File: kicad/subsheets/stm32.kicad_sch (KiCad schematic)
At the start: 12 parts, among them U3 STM32U575RGT6

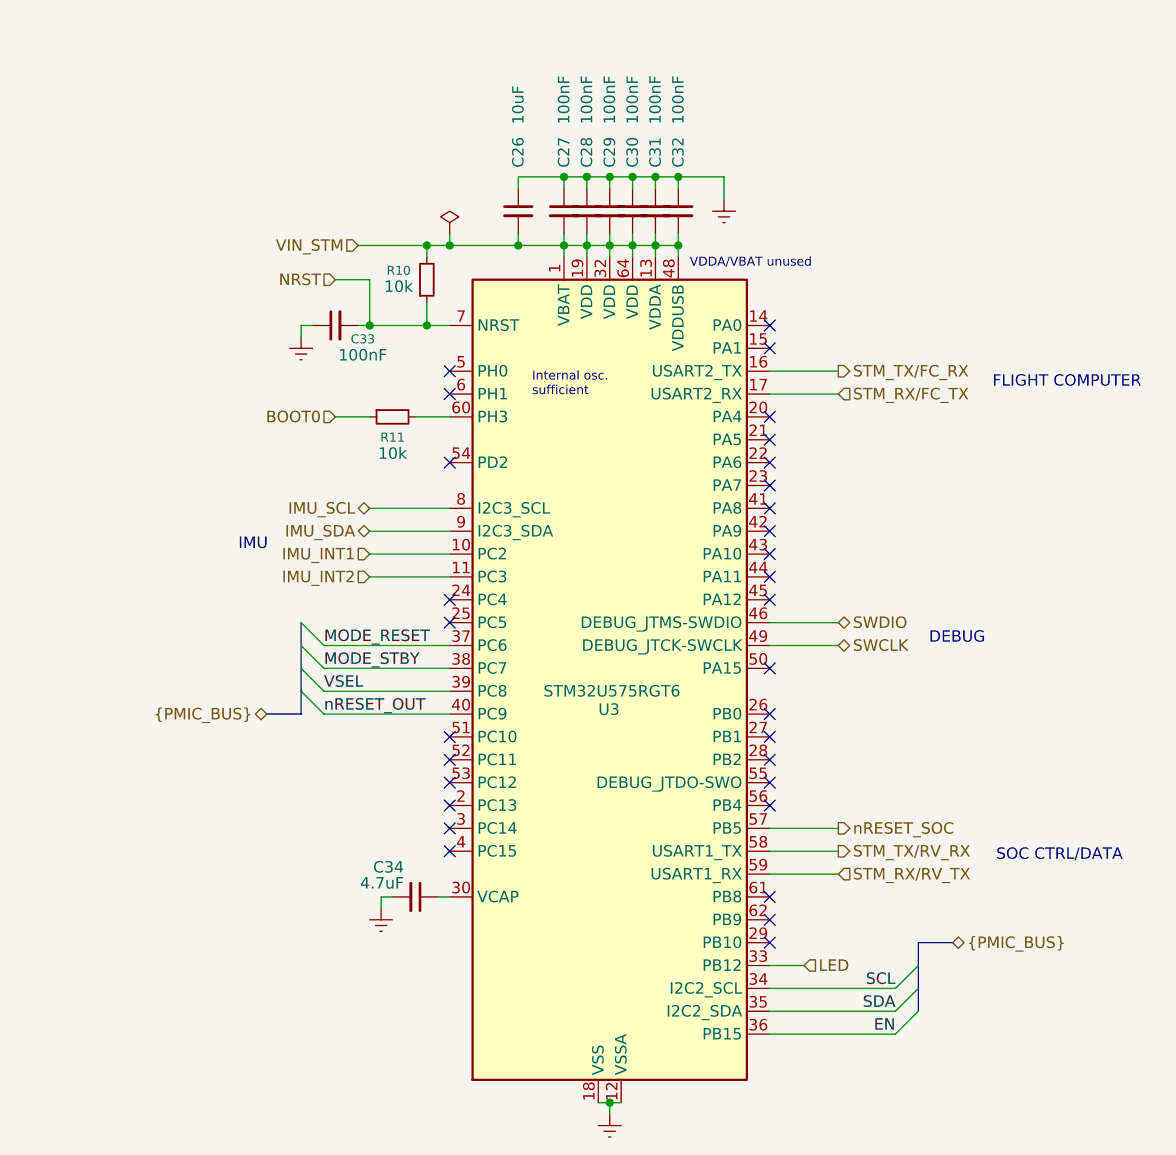
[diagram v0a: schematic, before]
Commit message: Switch to lower-cost STM32U0
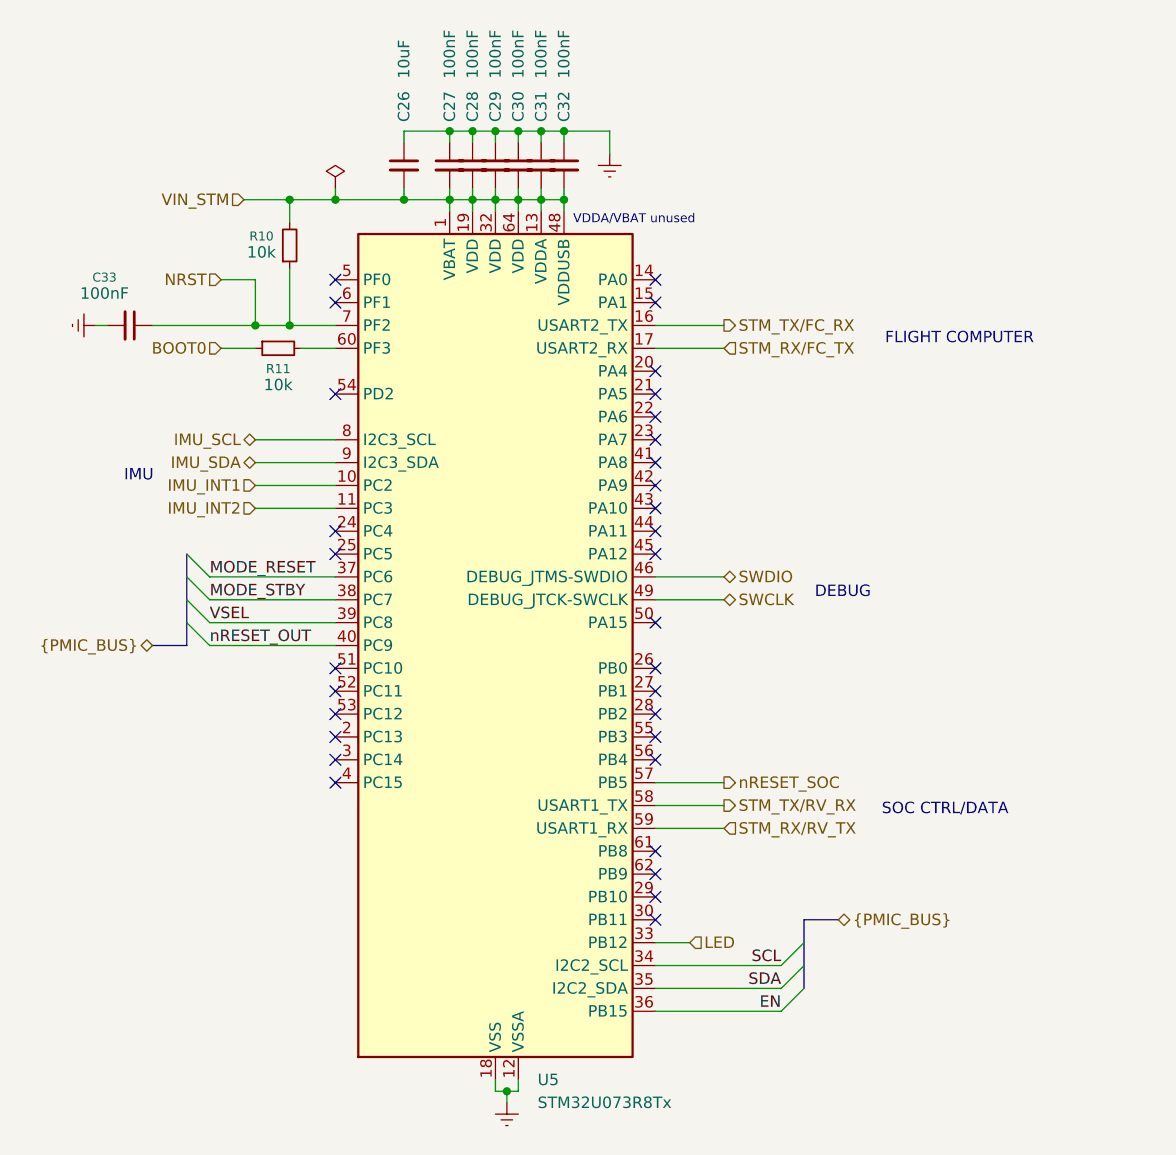
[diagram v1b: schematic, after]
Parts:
- removed C34: 4.7uF, Capacitor_SMD:C_0805_2012Metric, symbol Device:C_Small
- removed U3: STM32U575RGT6, Package_QFP:LQFP-64_10x10mm_P0.5mm, symbol MCU_ST_STM32U5:STM32U575RGTx
- added U5: STM32U073R8Tx, Package_QFP:LQFP-64_10x10mm_P0.5mm, symbol MCU_ST_STM32U0:STM32U073R8Tx
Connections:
- net EN: now also U5.36 (PB15)
- net GND: now also C33.2, U5.12 (VSSA), U5.18 (VSS), U5.31 (VSS), U5.47 (VSS), U5.63 (VSS); no longer C33.1
- net IMU_INT1: now also U5.10 (PC2)
- net IMU_INT2: now also U5.11 (PC3)
- net IMU_SCL: now also U5.8 (PC0)
- net IMU_SDA: now also U5.9 (PC1)
- net LED: now also U5.33 (PB12)
- net MODE_RESET: now also U5.37 (PC6)
- net MODE_STBY: now also U5.38 (PC7)
- net NRST: now also C33.1, U5.7 (PF2); no longer C33.2
- net SCL: now also U5.34 (PB13)
- net SDA: now also U5.35 (PB14)
- net STM_RX/FC_TX: now also U5.17 (PA3)
- net STM_RX/RV_TX: now also U5.59 (PB7)
- net STM_TX/FC_RX: now also U5.16 (PA2)
- net STM_TX/RV_RX: now also U5.58 (PB6)
- net SWCLK: now also U5.49 (PA14)
- net SWDIO: now also U5.46 (PA13)
- net VIN_STM: now also U5.1 (VBAT), U5.13 (VDDA), U5.19 (VDD), U5.32 (VDD), U5.48 (VDDUSB), U5.64 (VDD)
- net VSEL: now also U5.39 (PC8)
- net nRESET_OUT: now also U5.40 (PC9)
- net nRESET_SOC: now also U5.57 (PB5)
- net at R11.2: now also U5.60 (PF3)
- no-connect marks 31 -> 32
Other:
- note removed: "Internal osc. sufficient"
- moved on the sheet: C26, C27, C28, C29, C30, C31, C32, C33, R10, R11

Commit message: Add missing passives and microphone
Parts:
- renumbered U5 to U3
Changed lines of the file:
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@@
 	)
 	(junction
-		(at 127 49.53)
-		(diameter 0)
-		(color 0 0 0 0)
-	)
-	(junction
 		(at 149.86 49.53)
 		(diameter 0)
@@
 	(wire
 		(pts
-			(xy 121.92 49.53) (xy 127 49.53)
-		)
-		(stroke
-			(width 0)
-			(type default)
-		)
-	)
-	(wire
-		(pts
-			(xy 127 48.26) (xy 127 49.53)
+			(xy 121.92 49.53) (xy 134.62 49.53)
 		)
 		(stroke
@@
 	(wire
 		(pts
-			(xy 127 49.53) (xy 134.62 49.53)
-		)
-		(stroke
-			(width 0)
-			(type default)
-		)
-	)
-	(wire
-		(pts
 			(xy 170.18 116.84) (xy 162.56 116.84)
 		)
@@
 	)
 	(symbol
-		(lib_id "power:PWR_FLAG")
-		(at 127 48.26 0)
-		(unit 1)
-		(body_style 1)
-		(exclude_from_sim no)
-		(in_bom yes)
-		(on_board yes)
-		(in_pos_files yes)
-		(dnp no)
-		(property "Reference" "#FLG03"
-			(at 127 46.355 0)
-			(hide yes)
-			(show_name no)
-			(do_not_autoplace no)
-			(effects
-				(font
-					(size 1.27 1.27)
-				)
-			)
-		)
-		(property "Value" "PWR_FLAG"
-			(at 127 44.45 0)
-			(hide yes)
-			(show_name no)
-			(do_not_autoplace no)
-			(effects
-				(font
-					(size 1.27 1.27)
-				)
-			)
-		)
-		(property "Footprint" ""
-			(at 127 48.26 0)
-			(hide yes)
-			(show_name no)
-			(do_not_autoplace no)
-			(effects
-				(font
-					(size 1.27 1.27)
-				)
-			)
-		)
-		(property "Datasheet" ""
-			(at 127 48.26 0)
-			(hide yes)
-			(show_name no)
-			(do_not_autoplace no)
-			(effects
-				(font
-					(size 1.27 1.27)
-				)
-			)
-		)
-		(property "Description" "Special symbol for telling ERC where power comes from"
-			(at 127 48.26 0)
-			(hide yes)
-			(show_name no)
-			(do_not_autoplace no)
-			(effects
-				(font
-					(size 1.27 1.27)
-				)
-			)
-		)
-		(pin "1"
-		)
-		(instances
-			(project "a3-srad-camera-v2"
-				(path "/c4ff1aa6-4aa7-4de3-a597-83271e910ec4/f270ac7c-6fb9-4f92-b42e-3a719cd8dbad"
-					(reference "#FLG03")
-					(unit 1)
-				)
-			)
-		)
-	)
-	(symbol
 		(lib_id "Device:C_Small")
 		(at 144.78 45.72 0)
@@
 		(dnp no)
 		(fields_autoplaced yes)
-		(property "Reference" "U5"
+		(property "Reference" "U3"
 			(at 149.4633 147.32 0)
 			(show_name no)
@@
 			(project "a3-srad-camera-v2"
 				(path "/c4ff1aa6-4aa7-4de3-a597-83271e910ec4/f270ac7c-6fb9-4f92-b42e-3a719cd8dbad"
-					(reference "U5")
+					(reference "U3")
 					(unit 1)
 				)
@@
 		(in_pos_files yes)
 		(dnp no)
-		(property "Reference" "#PWR067"
+		(property "Reference" "#PWR030"
 			(at 93.98 63.5 0)
 			(hide yes)
@@
 			(project "a3-srad-camera-v2"
 				(path "/c4ff1aa6-4aa7-4de3-a597-83271e910ec4/f270ac7c-6fb9-4f92-b42e-3a719cd8dbad"
-					(reference "#PWR067")
+					(reference "#PWR030")
 					(unit 1)
 				)
@@
 		(in_pos_files yes)
 		(dnp no)
-		(property "Reference" "#PWR069"
+		(property "Reference" "#PWR031"
 			(at 146.05 156.21 0)
 			(hide yes)
@@
 			(project "a3-srad-camera-v2"
 				(path "/c4ff1aa6-4aa7-4de3-a597-83271e910ec4/f270ac7c-6fb9-4f92-b42e-3a719cd8dbad"
-					(reference "#PWR069")
+					(reference "#PWR031")
 					(unit 1)
 				)
@@
 		(in_pos_files yes)
 		(dnp no)
-		(property "Reference" "#PWR070"
+		(property "Reference" "#PWR029"
 			(at 157.48 50.8 0)
 			(hide yes)
@@
 			(project "a3-srad-camera-v2"
 				(path "/c4ff1aa6-4aa7-4de3-a597-83271e910ec4/f270ac7c-6fb9-4f92-b42e-3a719cd8dbad"
-					(reference "#PWR070")
+					(reference "#PWR029")
 					(unit 1)
 				)

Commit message: Footprint + silkscreen corrections
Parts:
- C26: renamed from C33; now left out of the parts list
- C27: renamed from C26; now left out of the parts list
- C28: renamed from C27; now left out of the parts list
- C29: renamed from C28; now left out of the parts list
- C30: renamed from C29; now left out of the parts list
- C31: renamed from C30; now left out of the parts list
- C32: renamed from C31; now left out of the parts list
- C33: renamed from C32; now left out of the parts list
- R10: renamed from R11; now left out of the parts list
- R11: renamed from R10; now left out of the parts list
- U3: now left out of the parts list

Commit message: Minor kicad changes
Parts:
- C26, C28, C29, C30, C31, C32, C33, R11, U3: BOARD_SIDE (none) -> Front; now in the parts list
- C27, R10: now in the parts list
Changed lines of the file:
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@@
 		(body_style 1)
 		(exclude_from_sim no)
-		(in_bom no)
+		(in_bom yes)
 		(on_board yes)
 		(in_pos_files yes)
@@
 			)
 		)
+		(property "BOARD_SIDE" "Front"
+			(at 142.24 45.72 90)
+			(hide yes)
+			(show_name no)
+			(do_not_autoplace no)
+			(effects
+				(font
+					(size 1.27 1.27)
+				)
+			)
+		)
 		(pin "2"
 		)
@@
 		(body_style 1)
 		(exclude_from_sim no)
-		(in_bom no)
+		(in_bom yes)
 		(on_board yes)
 		(in_pos_files yes)
@@
 			)
 		)
+		(property "BOARD_SIDE" ""
+			(at 120.65 66.04 90)
+			(hide yes)
+			(show_name no)
+			(do_not_autoplace no)
+			(effects
+				(font
+					(size 1.27 1.27)
+				)
+			)
+		)
 		(pin "2"
 		)
@@
 		(body_style 1)
 		(exclude_from_sim no)
-		(in_bom no)
+		(in_bom yes)
 		(on_board yes)
 		(in_pos_files yes)
@@
 			)
 		)
+		(property "BOARD_SIDE" "Front"
+			(at 144.78 45.72 90)
+			(hide yes)
+			(show_name no)
+			(do_not_autoplace no)
+			(effects
+				(font
+					(size 1.27 1.27)
+				)
+			)
+		)
 		(pin "2"
 		)
@@
 		(body_style 1)
 		(exclude_from_sim no)
-		(in_bom no)
+		(in_bom yes)
 		(on_board yes)
 		(in_pos_files yes)
@@
 			)
 		)
+		(property "BOARD_SIDE" "Front"
+			(at 144.78 99.06 0)
+			(hide yes)
+			(show_name no)
+			(do_not_autoplace no)
+			(effects
+				(font
+					(size 1.27 1.27)
+				)
+			)
+		)
 		(pin "63"
 		)
@@
 		(body_style 1)
 		(exclude_from_sim no)
-		(in_bom no)
+		(in_bom yes)
 		(on_board yes)
 		(in_pos_files yes)
@@
 			)
 		)
+		(property "BOARD_SIDE" ""
+			(at 134.62 45.72 90)
+			(hide yes)
+			(show_name no)
+			(do_not_autoplace no)
+			(effects
+				(font
+					(size 1.27 1.27)
+				)
+			)
+		)
 		(pin "2"
 		)
@@
 		(body_style 1)
 		(exclude_from_sim no)
-		(in_bom no)
+		(in_bom yes)
 		(on_board yes)
 		(in_pos_files yes)
@@
 			)
 		)
+		(property "BOARD_SIDE" "Front"
+			(at 152.4 45.72 90)
+			(hide yes)
+			(show_name no)
+			(do_not_autoplace no)
+			(effects
+				(font
+					(size 1.27 1.27)
+				)
+			)
+		)
 		(pin "2"
 		)
@@
 		(body_style 1)
 		(exclude_from_sim no)
-		(in_bom no)
+		(in_bom yes)
 		(on_board yes)
 		(in_pos_files yes)
@@
 			)
 		)
+		(property "BOARD_SIDE" "Front"
+			(at 104.14 63.5 90)
+			(hide yes)
+			(show_name no)
+			(do_not_autoplace no)
+			(effects
+				(font
+					(size 1.27 1.27)
+				)
+			)
+		)
 		(pin "2"
 		)
@@
 		(body_style 1)
 		(exclude_from_sim no)
-		(in_bom no)
+		(in_bom yes)
 		(on_board yes)
 		(in_pos_files yes)
@@
 			)
 		)
+		(property "BOARD_SIDE" "Front"
+			(at 149.86 45.72 90)
+			(hide yes)
+			(show_name no)
+			(do_not_autoplace no)
+			(effects
+				(font
+					(size 1.27 1.27)
+				)
+			)
+		)
 		(pin "2"
 		)
@@
 		(body_style 1)
 		(exclude_from_sim no)
-		(in_bom no)
+		(in_bom yes)
 		(on_board yes)
 		(in_pos_files yes)
@@
 			)
 		)
+		(property "BOARD_SIDE" "Front"
+			(at 147.32 45.72 90)
+			(hide yes)
+			(show_name no)
+			(do_not_autoplace no)
+			(effects
+				(font
+					(size 1.27 1.27)
+				)
+			)
+		)
 		(pin "2"
 		)
@@
 		(body_style 1)
 		(exclude_from_sim no)
-		(in_bom no)
+		(in_bom yes)
 		(on_board yes)
 		(in_pos_files yes)
@@
 			)
 		)
+		(property "BOARD_SIDE" "Front"
+			(at 121.92 54.61 0)
+			(hide yes)
+			(show_name no)
+			(do_not_autoplace no)
+			(effects
+				(font
+					(size 1.27 1.27)
+				)
+			)
+		)
 		(pin "1"
 		)
@@
 		(body_style 1)
 		(exclude_from_sim no)
-		(in_bom no)
+		(in_bom yes)
 		(on_board yes)
 		(in_pos_files yes)
@@
 			(at 139.7 45.72 90)
 			(hide yes)
+			(show_name no)
+			(do_not_autoplace no)
+			(effects
+				(font
+					(size 1.27 1.27)
+				)
+			)
+		)
+		(property "BOARD_SIDE" "Front"
+			(at 139.7 45.72 90)
+			(hide yes)
